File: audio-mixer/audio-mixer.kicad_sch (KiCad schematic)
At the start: 45 parts, among them J1 Input A1, J10 Pot, J11 Input B3, J12 Pot, J13 Pot, J14 Output A, J15 Pot, J16 Output B, J17 AudioJack4, J18 Power, J19 Power, J2 Pot, J3 Input A2, J4 Pot, J5 Input A3, J6 Pot, J7 Input B1, J8 Pot, J9 Input B2, SW1 Mono/Stereo, U1 TL072

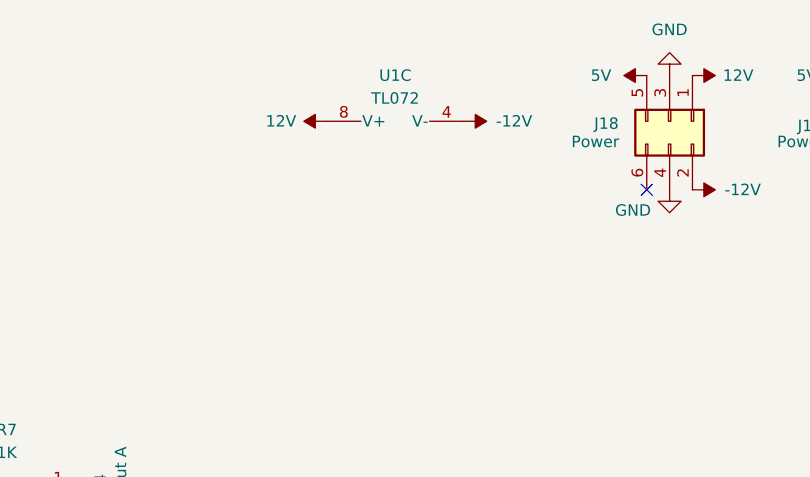
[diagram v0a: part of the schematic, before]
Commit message: More space for backup pot
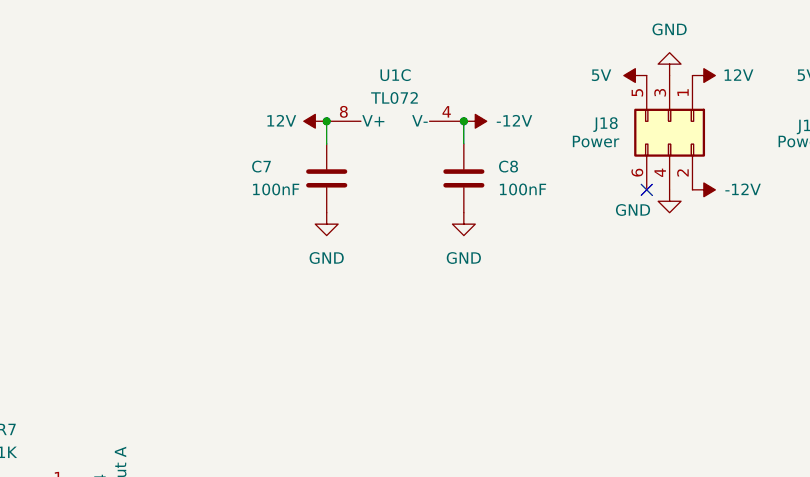
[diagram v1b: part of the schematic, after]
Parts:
- added C7, C8: 100nF, Capacitor_THT:C_Disc_D4.3mm_W1.9mm_P5.00mm, symbol Device:C
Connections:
- net -12V: now also C8.2
- net 12V: now also C7.2
- net GND: now also C7.1, C8.1

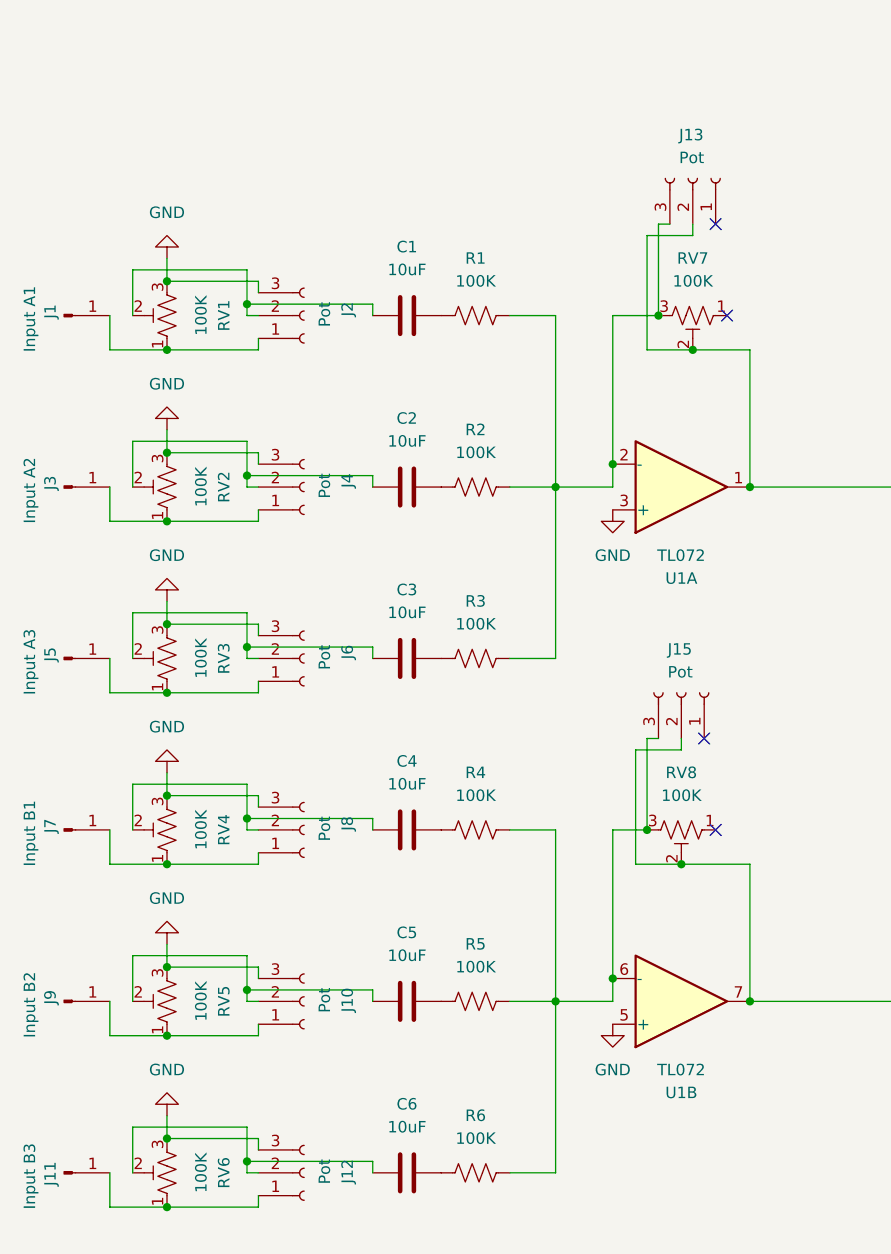
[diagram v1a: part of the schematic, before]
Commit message: Fix issues with audio mixer
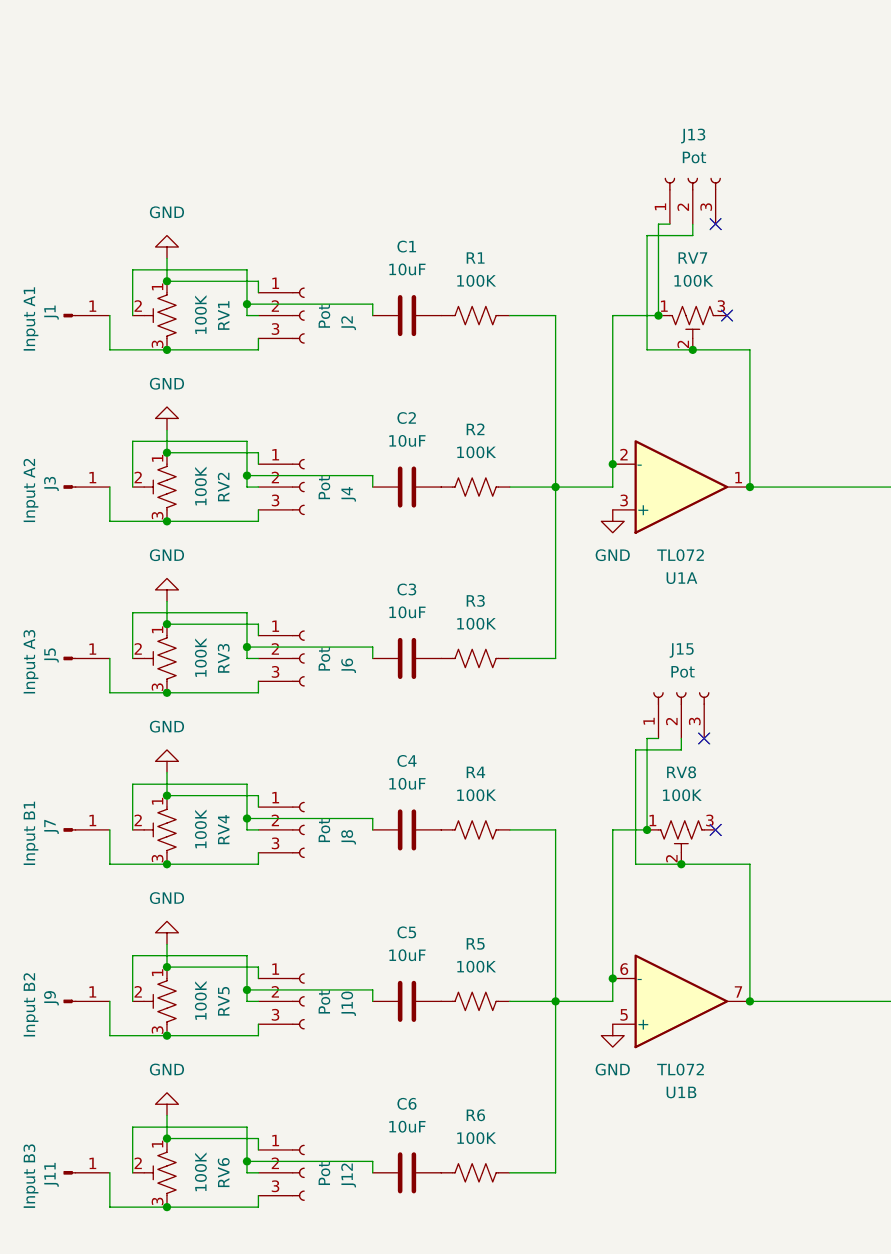
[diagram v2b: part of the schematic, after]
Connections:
- net GND: now also J10.1 (Pin_1), J12.1 (Pin_1), J2.1 (Pin_1), J4.1 (Pin_1), J6.1 (Pin_1), J8.1 (Pin_1), RV1.1, RV2.1, RV3.1, RV4.1, RV5.1, RV6.1; no longer J10.3 (Pin_3), J12.3 (Pin_3), J2.3 (Pin_3), J4.3 (Pin_3), J6.3 (Pin_3), J8.3 (Pin_3), RV1.3, RV2.3, RV3.3, RV4.3, RV5.3, RV6.3
- net at R1.2, R2.2, R3.2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: now also J13.1 (Pin_1), RV7.1; no longer J13.3 (Pin_3), RV7.3
- net at J15.1 (Pin_1): now also R4.2, R5.2, R6.2, RV8.1, U1.6 (-)
- new net: J1.1 (Pin_1), J2.3 (Pin_3), RV1.3
- new net: J3.1 (Pin_1), J4.3 (Pin_3), RV2.3
- new net: J5.1 (Pin_1), J6.3 (Pin_3), RV3.3
- new net: J7.1 (Pin_1), J8.3 (Pin_3), RV4.3
- new net: J10.3 (Pin_3), J9.1 (Pin_1), RV5.3
- new net: J11.1 (Pin_1), J12.3 (Pin_3), RV6.3
- now unconnected: J15.3 (Pin_3), RV8.3
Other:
- moved on the sheet: J13, J15, RV1, RV2, RV3, RV4, RV5, RV6, RV7, RV8
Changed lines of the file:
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@@
 		(lib_id "Connector:Conn_01x03_Socket")
 		(at 95.25 49.53 0)
-		(mirror x)
 		(unit 1)
 		(exclude_from_sim no)
@@
 		(dnp no)
 		(property "Reference" "J2"
-			(at 100.076 48.006 90)
+			(at 100.076 51.054 90)
 			(effects
 				(font
@@
 		)
 		(property "Value" "Pot"
-			(at 97.536 48.006 90)
+			(at 97.536 51.054 90)
 			(effects
 				(font
@@
 	(symbol
 		(lib_id "Device:R_Potentiometer_Trim_US")
-		(at 80.01 49.53 180)
+		(at 80.01 49.53 0)
+		(mirror y)
 		(unit 1)
 		(exclude_from_sim no)
@@
 	(symbol
 		(lib_id "Device:R_Potentiometer_Trim_US")
-		(at 80.01 68.58 180)
+		(at 80.01 68.58 0)
+		(mirror y)
 		(unit 1)
 		(exclude_from_sim no)
@@
 		(lib_id "Connector:Conn_01x03_Socket")
 		(at 95.25 144.78 0)
-		(mirror x)
 		(unit 1)
 		(exclude_from_sim no)
@@
 		(dnp no)
 		(property "Reference" "J12"
-			(at 100.076 143.256 90)
+			(at 100.076 146.304 90)
 			(effects
 				(font
@@
 		)
 		(property "Value" "Pot"
-			(at 97.536 143.256 90)
+			(at 97.536 146.304 90)
 			(effects
 				(font
@@
 	(symbol
 		(lib_id "Connector:Conn_01x03_Socket")
-		(at 137.16 91.44 270)
-		(mirror x)
+		(at 137.16 91.44 90)
 		(unit 1)
 		(exclude_from_sim no)
@@
 		(dnp no)
 		(property "Reference" "J15"
-			(at 135.636 86.614 90)
+			(at 138.684 86.614 90)
 			(effects
 				(font
@@
 		)
 		(property "Value" "Pot"
-			(at 135.636 89.154 90)
+			(at 138.684 89.154 90)
 			(effects
 				(font
@@
 		(lib_id "Connector:Conn_01x03_Socket")
 		(at 95.25 87.63 0)
-		(mirror x)
 		(unit 1)
 		(exclude_from_sim no)
@@
 		(dnp no)
 		(property "Reference" "J6"
-			(at 100.076 86.106 90)
+			(at 100.076 89.154 90)
 			(effects
 				(font
@@
 		)
 		(property "Value" "Pot"
-			(at 97.536 86.106 90)
+			(at 97.536 89.154 90)
 			(effects
 				(font
@@
 	(symbol
 		(lib_id "Device:R_Potentiometer_Trim_US")
-		(at 80.01 87.63 180)
+		(at 80.01 87.63 0)
+		(mirror y)
 		(unit 1)
 		(exclude_from_sim no)
@@
 	(symbol
 		(lib_id "Device:R_Potentiometer_Trim_US")
-		(at 137.16 106.68 270)
+		(at 137.16 106.68 90)
+		(mirror x)
 		(unit 1)
 		(exclude_from_sim no)
@@
 	(symbol
 		(lib_id "Device:R_Potentiometer_Trim_US")
-		(at 138.43 49.53 270)
+		(at 138.43 49.53 90)
+		(mirror x)
 		(unit 1)
 		(exclude_from_sim no)
@@
 		(lib_id "Connector:Conn_01x03_Socket")
 		(at 95.25 125.73 0)
-		(mirror x)
 		(unit 1)
 		(exclude_from_sim no)
@@
 		(dnp no)
 		(property "Reference" "J10"
-			(at 100.076 124.206 90)
+			(at 100.076 127.254 90)
 			(effects
 				(font
@@
 		)
 		(property "Value" "Pot"
-			(at 97.536 124.206 90)
+			(at 97.536 127.254 90)
 			(effects
 				(font
@@
 		(lib_id "Connector:Conn_01x03_Socket")
 		(at 95.25 106.68 0)
-		(mirror x)
 		(unit 1)
 		(exclude_from_sim no)
@@
 		(dnp no)
 		(property "Reference" "J8"
-			(at 100.076 105.156 90)
+			(at 100.076 108.204 90)
 			(effects
 				(font
@@
 		)
 		(property "Value" "Pot"
-			(at 97.536 105.156 90)
+			(at 97.536 108.204 90)
 			(effects
 				(font
@@
 	(symbol
 		(lib_id "Connector:Conn_01x03_Socket")
-		(at 138.43 34.29 270)
-		(mirror x)
+		(at 138.43 34.29 90)
 		(unit 1)
 		(exclude_from_sim no)
@@
 		(dnp no)
 		(property "Reference" "J13"
-			(at 136.906 29.464 90)
+			(at 139.954 29.464 90)
 			(effects
 				(font
@@
 		)
 		(property "Value" "Pot"
-			(at 136.906 32.004 90)
+			(at 139.954 32.004 90)
 			(effects
 				(font
@@
 	(symbol
 		(lib_id "Device:R_Potentiometer_Trim_US")
-		(at 80.01 106.68 180)
+		(at 80.01 106.68 0)
+		(mirror y)
 		(unit 1)
 		(exclude_from_sim no)
@@
 	(symbol
 		(lib_id "Device:R_Potentiometer_Trim_US")
-		(at 80.01 144.78 180)
+		(at 80.01 144.78 0)
+		(mirror y)
 		(unit 1)
 		(exclude_from_sim no)
@@
 		(lib_id "Connector:Conn_01x03_Socket")
 		(at 95.25 68.58 0)
-		(mirror x)
 		(unit 1)
 		(exclude_from_sim no)
@@
 		(dnp no)
 		(property "Reference" "J4"
-			(at 100.076 67.056 90)
+			(at 100.076 70.104 90)
 			(effects
 				(font
@@
 		)
 		(property "Value" "Pot"
-			(at 97.536 67.056 90)
+			(at 97.536 70.104 90)
 			(effects
 				(font
@@
 	(symbol
 		(lib_id "Device:R_Potentiometer_Trim_US")
-		(at 80.01 125.73 180)
+		(at 80.01 125.73 0)
+		(mirror y)
 		(unit 1)
 		(exclude_from_sim no)

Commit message: Various fixes
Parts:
- added J20: Power, Connector_IDC:IDC-Header_2x03_P2.54mm_Vertical, symbol Connector_Generic:Conn_02x03_Odd_Even
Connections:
- net -12V: now also J20.2 (Pin_2)
- net 12V: now also J20.1 (Pin_1)
- net 5V: now also J20.5 (Pin_5)
- net GND: now also J20.3 (Pin_3), J20.4 (Pin_4)
- no-connect marks 7 -> 8
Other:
- moved on the sheet: C7, C8, J18, J19, U1C

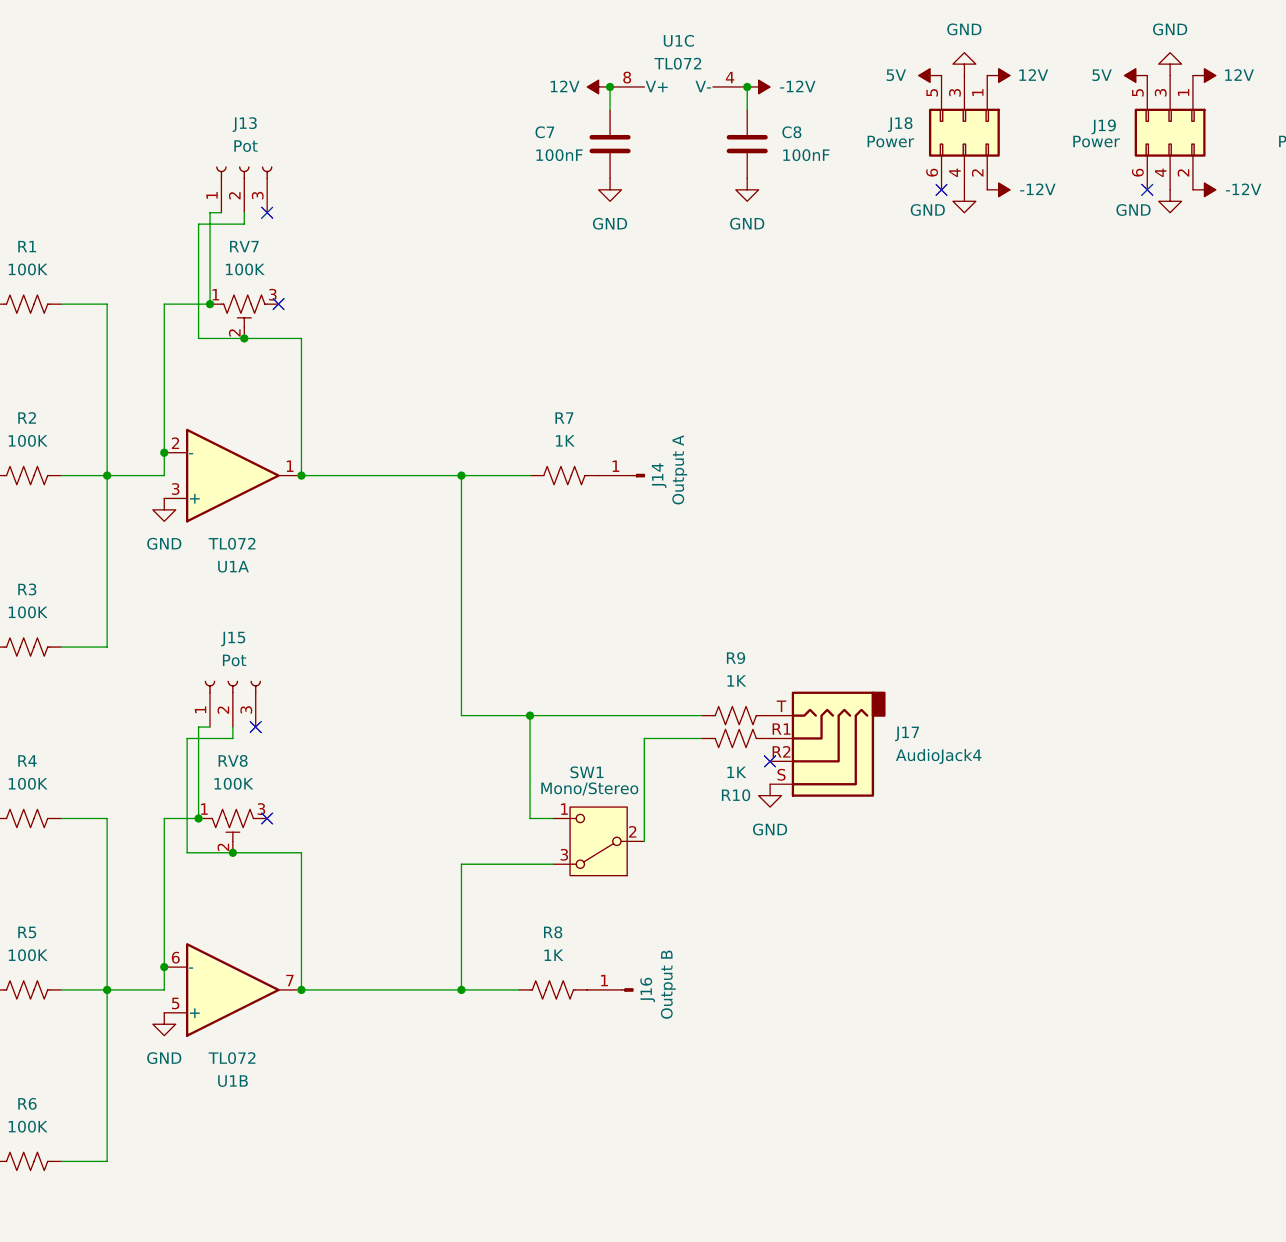
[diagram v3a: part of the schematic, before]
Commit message: Fix inverted output in audio mixer
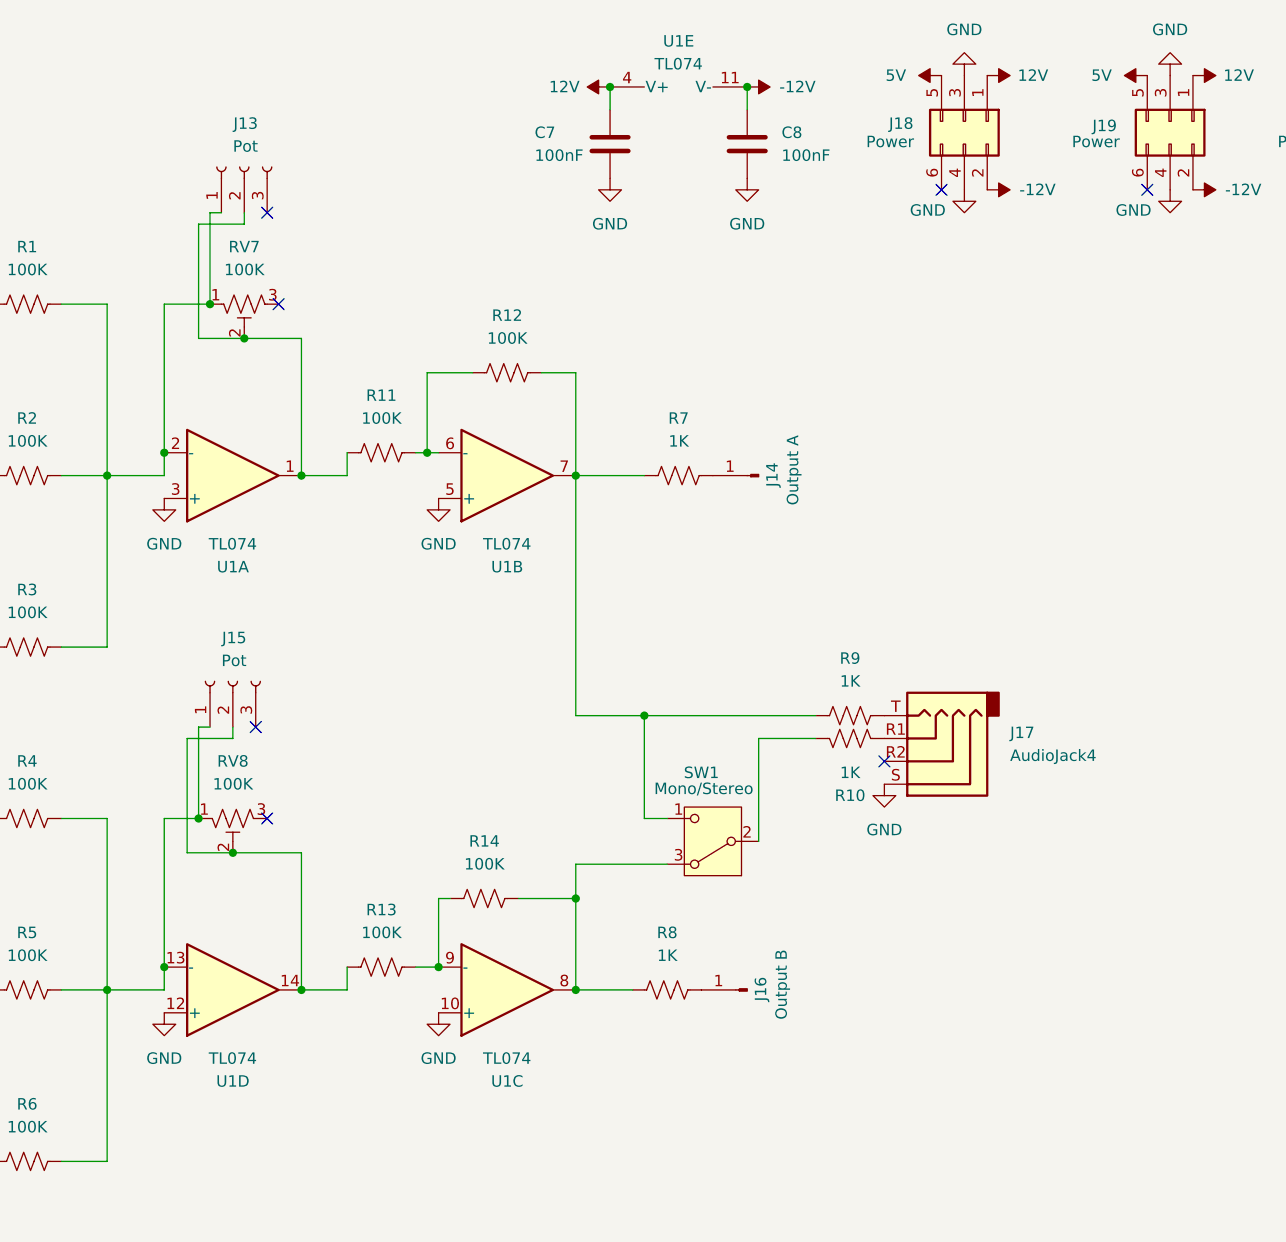
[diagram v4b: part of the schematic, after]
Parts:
- removed U1: TL072, Package_DIP:DIP-8_W7.62mm_Socket, symbol Amplifier_Operational:TL072
- added R11, R12, R13, R14: 100K, Resistor_THT:R_Axial_DIN0207_L6.3mm_D2.5mm_P10.16mm_Horizontal, symbol Device:R_US
- added U1: TL074, Package_DIP:DIP-14_W7.62mm_Socket, symbol Amplifier_Operational:TL074
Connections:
- net -12V: now also U1.11 (V-)
- net 12V: now also U1.4 (V+)
- net GND: now also U1.10 (+), U1.12 (+), U1.3 (+), U1.5 (+)
- net at J13.1 (Pin_1), R1.2, R2.2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: now also U1.2 (-)
- net at J15.1 (Pin_1), R4.2, R5.2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: now also U1.13 (-)
- net at R8.1, SW1.3 (A): now also R14.2, U1.8; no longer J15.2 (Pin_2), RV8.2
- net at R7.1, R9.1, SW1.1 (C): now also R12.2, U1.7; no longer J13.2 (Pin_2), RV7.2
- new net: R11.2, R12.1, U1.6 (-)
- new net: R13.2, R14.1, U1.9 (-)
- new net: J15.2 (Pin_2), R13.1, RV8.2, U1.14
- new net: J13.2 (Pin_2), R11.1, RV7.2, U1.1
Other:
- moved on the sheet: J14, J16, J17, R10, R7, R8, R9, SW1
